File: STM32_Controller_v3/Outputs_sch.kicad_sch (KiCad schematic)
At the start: 26 parts, among them CN2 WJ15EDGVC-3.5-05P-14-00A, Q10 SMMBT5551LT1G, Q11 SMMBT5551LT1G, Q12 SMMBT5551LT1G, Q9 SMMBT5551LT1G

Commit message: production version
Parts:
- removed CN2: WJ15EDGVC-3.5-05P-14-00A, Library:PhoenixContact_MCV_1,5_5-G-3.5_1x05_P3.50mm_Vertical, symbol Library:CN_Header_3.5mm_5W_180_300V
- removed CNP2: WJ15EDGK-3.5-05P-14-00A, symbol Library:CN_Plug_3.5mm_5W_180_300V
- added CN2: WJ15EDGVC-3.81-05P-14-00A, Library:PhoenixContact_MCV_1,5_5-G-3.81_1x05_P3.81mm_Vertical, symbol Library:CN_Header_3.81mm_5W_180_300V
- added CNP2: WJ15EDGK-3.81-05P-14-00A, symbol Library:CN_Plug_3.81mm_5W_180_300V
- D1, D2, D3, D4: Assembly (none) -> SMT; Manufacturer (none) -> Changzhou Starsea Elec; Part.Number (none) -> LL4148
- LD10, LD11, LD12, LD9: Assembly (none) -> SMT; Manufacturer (none) -> NATIONSTAR; Part.Number (none) -> NCD0805R1
- Q10, Q11, Q12, Q9: Assembly (none) -> SMT; Manufacturer (none) -> JSCJ; Part.Number (none) -> MMBT5551
- R33, R34, R37, R38, R41, R42, R45, R46: Assembly (none) -> SMT; Manufacturer (none) -> UNI-ROYAL; Part.Number (none) -> 0805W8F1001T5E
- R39, R40, R47, R48: Assembly (none) -> SMT; Manufacturer (none) -> UNI-ROYAL; Part.Number (none) -> 0805W8F1002T5E
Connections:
- net +V_IN: now also CN2.1 (Pin_1)
- net OUT1: now also CN2.5 (Pin_5)
- net OUT2: now also CN2.4 (Pin_4)
- net OUT3: now also CN2.3 (Pin_3)
- net OUT4: now also CN2.2 (Pin_2)

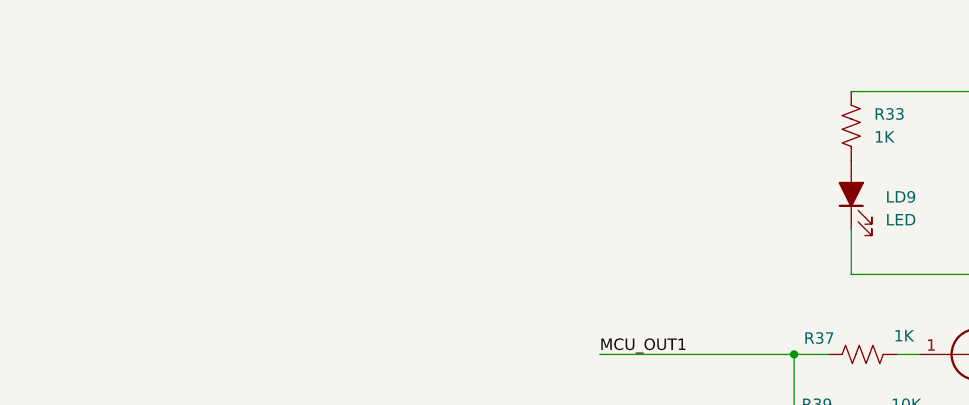
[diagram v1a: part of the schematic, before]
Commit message: update dimension information
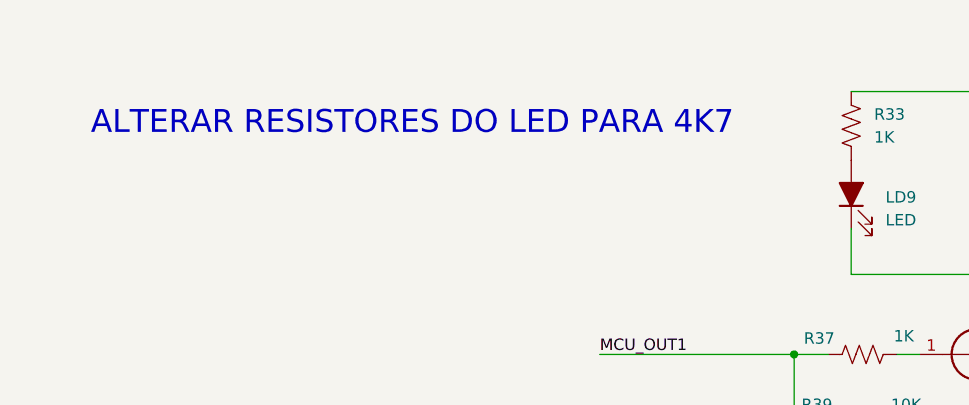
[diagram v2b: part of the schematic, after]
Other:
- note added: "ALTERAR RESISTORES DO LED PARA 4K7"
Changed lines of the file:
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@@
 		(comment 2 "29/08/2025")
+	)
+	(text "ALTERAR RESISTORES DO LED PARA 4K7"
+		(exclude_from_sim no)
+		(at 61.722 23.876 0)
+		(effects
+			(font
+				(size 2.54 2.54)
+			)
+		)
 	)
 	(junction

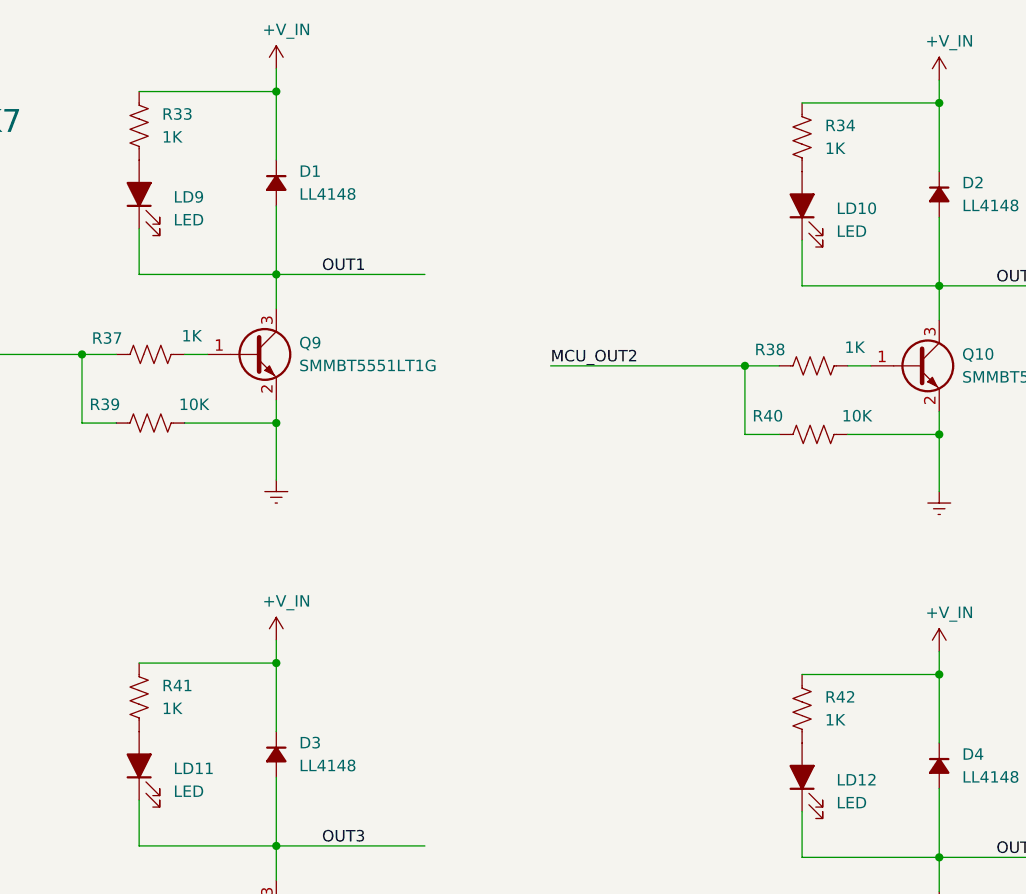
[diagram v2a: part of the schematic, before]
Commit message: res 4k7 in digital inputs and outputs leds
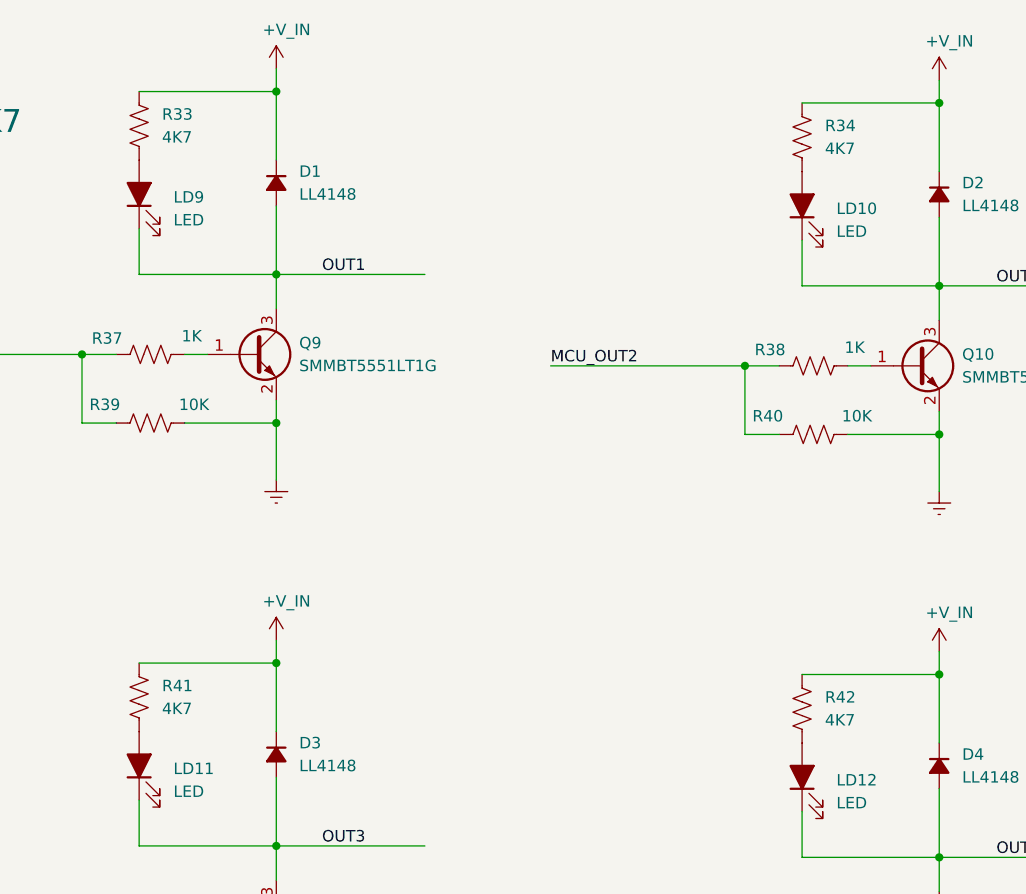
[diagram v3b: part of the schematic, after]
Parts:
- removed R33, R34, R41, R42: 1K, Library:R_0805, symbol Library:R_0805_1K_1P
- added R33, R34, R41, R42: 4K7, db_resistors:R_0805, symbol Library:R_0805_4K7_1P
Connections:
- net +V_IN: now also R33.1, R34.1, R41.1, R42.1
- net at LD11.2 (A): now also R41.2
- net at LD12.2 (A): now also R42.2
- net at LD9.2 (A): now also R33.2
- net at LD10.2 (A): now also R34.2
